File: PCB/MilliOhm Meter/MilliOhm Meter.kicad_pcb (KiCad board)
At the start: 2 copper layers, 43 parts, among them J1 - 9V in +, J2 Conn_01x01_Pin, J3 Conn_01x01_Pin, J4 Conn_01x01_Pin, J5 Conn_01x01_Pin, J6 Conn_01x01_Pin, J7 Conn_01x01_Pin, J8 Conn_01x01_Pin, J9 Conn_01x01_Pin, SW1 SW_SPST, U2 LT3092xST, U3 LT1634-1.25, U4 MAX680CPA+, U5 INA106U

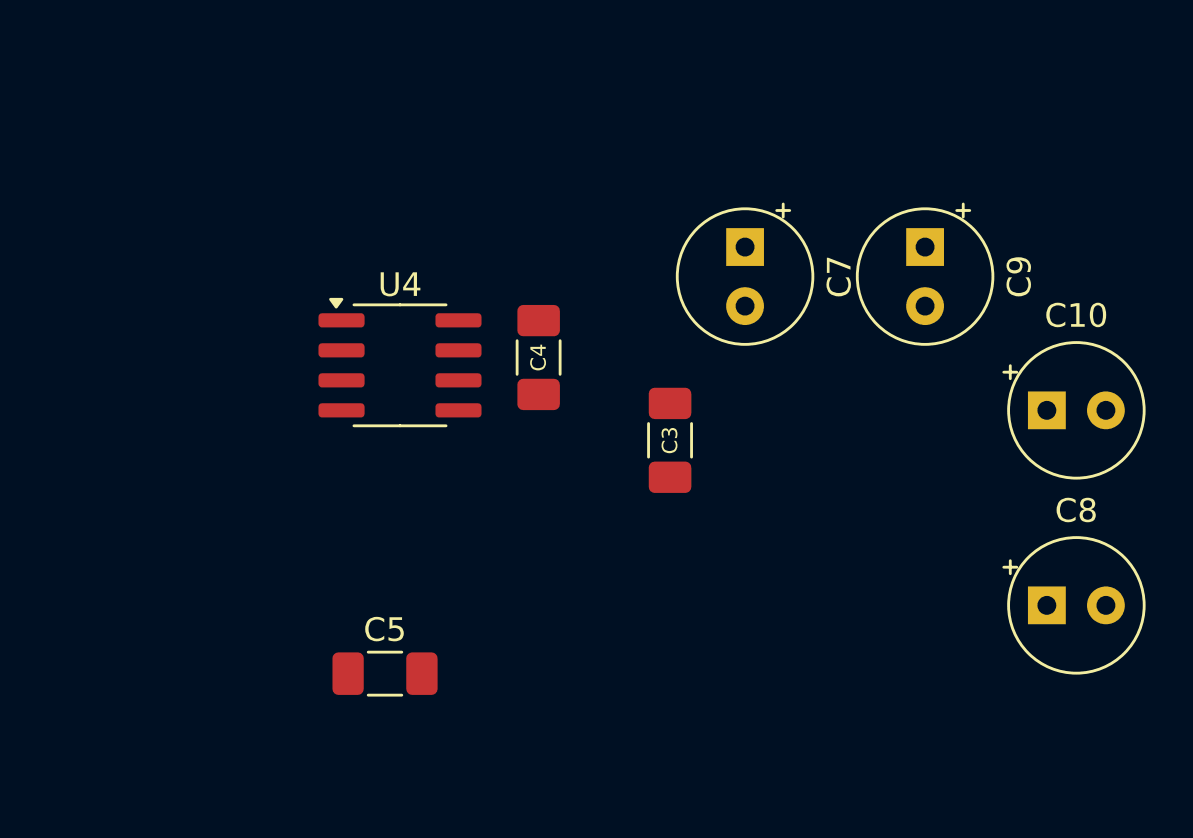
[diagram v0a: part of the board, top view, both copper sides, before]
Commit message: DC charge pump layout
PCB update
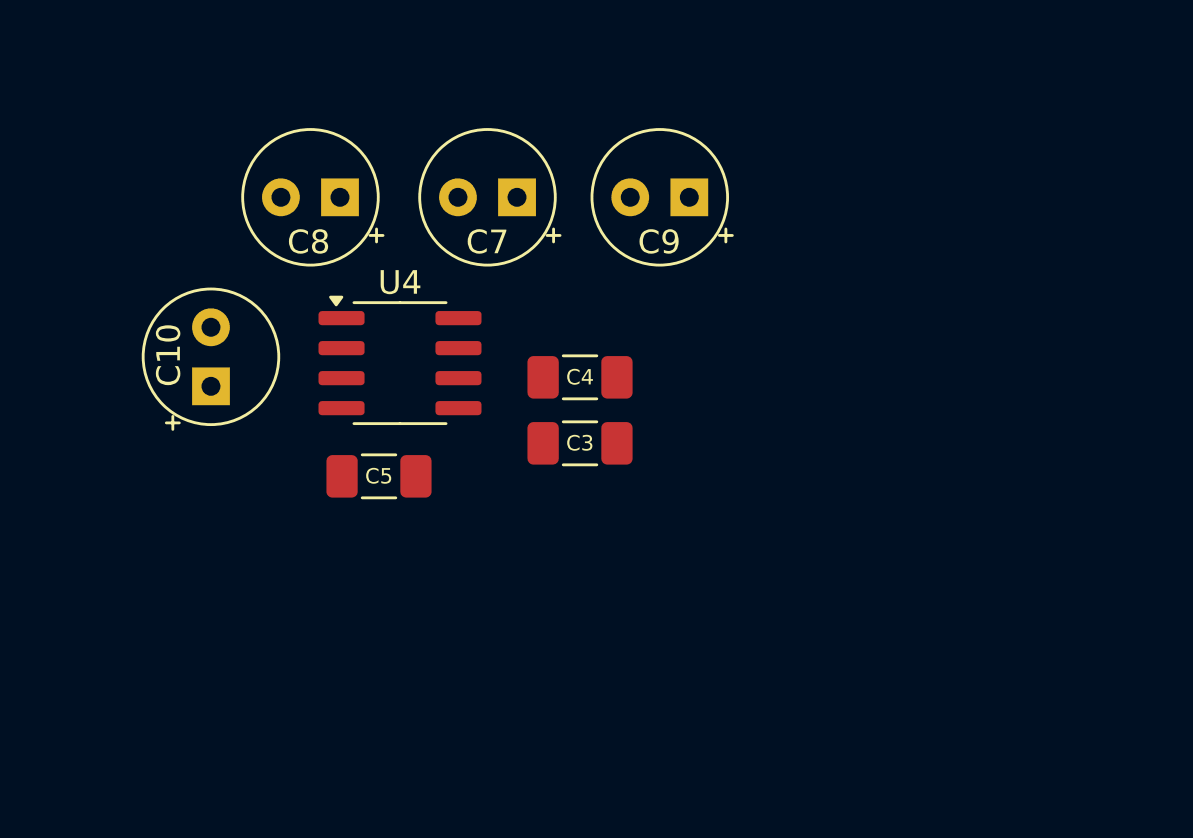
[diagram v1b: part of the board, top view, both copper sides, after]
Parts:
- moved C10 35.4 mm to (207.3, 44.7), turned to 90 degrees
- moved C8 34.5 mm to (212.7, 36.7), turned to 180 degrees
- moved C9 10.2 mm to (227.5, 36.7), turned to 180 degrees
- moved C7 9.88 mm to (220.2, 36.7), turned to 180 degrees
- moved C5 8.35 mm to (214.4, 48.5)
- moved C3 3.81 mm to (222.9, 47.1), turned to 180 degrees
- moved C4 1.94 mm to (222.9, 44.3), turned to 0 degrees
- moved U4 0.09 mm to (215.3, 43.7)

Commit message: PCB Progress
Component layout complete, board outline complete, routing in progress.
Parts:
- moved H2 175.4 mm to (101.6, 94.0)
- moved C9 170.5 mm to (58.4, 58.4), turned to 0 degrees
- moved C4 168.5 mm to (55.8, 65.6), turned to 90 degrees
- moved C10 168.4 mm to (40.3, 66.4)
- moved C7 168.4 mm to (53.2, 58.4)
- moved C8 168.4 mm to (45.7, 58.4)
- moved U4 168.4 mm to (48.3, 65.4)
- moved H3 167.4 mm to (101.6, 57.1)
- moved C3 164.9 mm to (59.1, 65.6), turned to 90 degrees
- moved C5 153.0 mm to (62.4, 65.6), turned to 90 degrees
- moved J1 119.7 mm to (54.9, 95.2), turned to 0 degrees
- moved C1 115.5 mm to (58.9, 90.2), turned to 0 degrees
- moved SW1 114.9 mm to (47.4, 95.2), turned to 180 degrees
- moved H4 110.4 mm to (36.8, 94.0)
- moved F1 107.3 mm to (44.0, 90.2), turned to 0 degrees
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- renumbered R6 to 0R, J2 to Current+, J3 to Current-, RV2 to RV100K, RV1 to RV100R, J5 to Sense+, J4 to Sense-, J8 to VO+, J9 to VO-
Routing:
- net /-10V: track 0.00 -> 95.3 mm
- net +5V: track 0.00 -> 64.7 mm, vias 0 -> 2
- net /+10V: track 0.00 -> 47.9 mm
- net GND: track 0.00 -> 20.6 mm, vias 0 -> 1
- net /VO-: track 0.00 -> 15.1 mm
- net /VO+: track 0.00 -> 14.7 mm
- net /Sense-: track 0.00 -> 14.2 mm
- net Net-(U1-VI): track 0.00 -> 13.7 mm
- net Net-(R8-Pad1): track 0.00 -> 13.0 mm
- net /Sense+: track 0.00 -> 10.7 mm
- net Net-(U4-C1+): track 0.00 -> 9.62 mm
- net Net-(U4-C2-): track 0.00 -> 9.29 mm
- net Net-(U4-C2+): track 0.00 -> 8.75 mm
- net Net-(U4-C1-): track 0.00 -> 7.84 mm
- net Net-(J1-Pin_1): track 0.00 -> 7.58 mm
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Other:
- board outline added: 72.4 x 44.5 mm
- board text added: "(Shield from caps)"
- board text added: "+/- 10V PS"
- board text added: "10X Precision Amplifier"
- board text added: "5V Regulator"
- board text added: "MilliOhm Meter - V01 - DK 4-16-24"

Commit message: First Draft PCB done
Revision 1 of the PCB is done, next step will be the probe design
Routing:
- net +5V: track 64.7 -> 130.4 mm, vias 2 -> 6
- net /Current+: track 0.00 -> 44.8 mm
- net (no net): track 0.00 -> 41.9 mm, vias 13 -> 45
- net Net-(R1-Pad1): track 0.00 -> 17.9 mm
- net GND: track 20.6 -> 32.2 mm, vias 1 -> 9
- net /Current-: track 0.00 -> 6.89 mm
- net Net-(R5-Pad2): track 0.00 -> 5.55 mm
- net Net-(U3-K): track 0.00 -> 4.25 mm
- net /-10V: track 95.3 -> 94.7 mm
- added copper zone on B.Cu, net GND
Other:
- board text added: "C1-C5: 0.1uF (1206) C6: 220uF 25v (THT) C7-C10: 22uF 16V (THT) C11: 0.1uF (1206)"
- board text added: "Current Source 100mA"
- board text added: "R1-R4: 56R2 R5: 63R4 R6, R10: 0R R7: 10R R8: 499K R9: 100R"
- board text added: "U1: LM2940 U2: LT3092 U3: LT1634-1.25 U4: MAX680 U5: INA106"
